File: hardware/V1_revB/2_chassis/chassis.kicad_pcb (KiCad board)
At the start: 2 copper layers, 39.1 x 31.7 mm, 18 parts, among them SW3 NKK_NR01

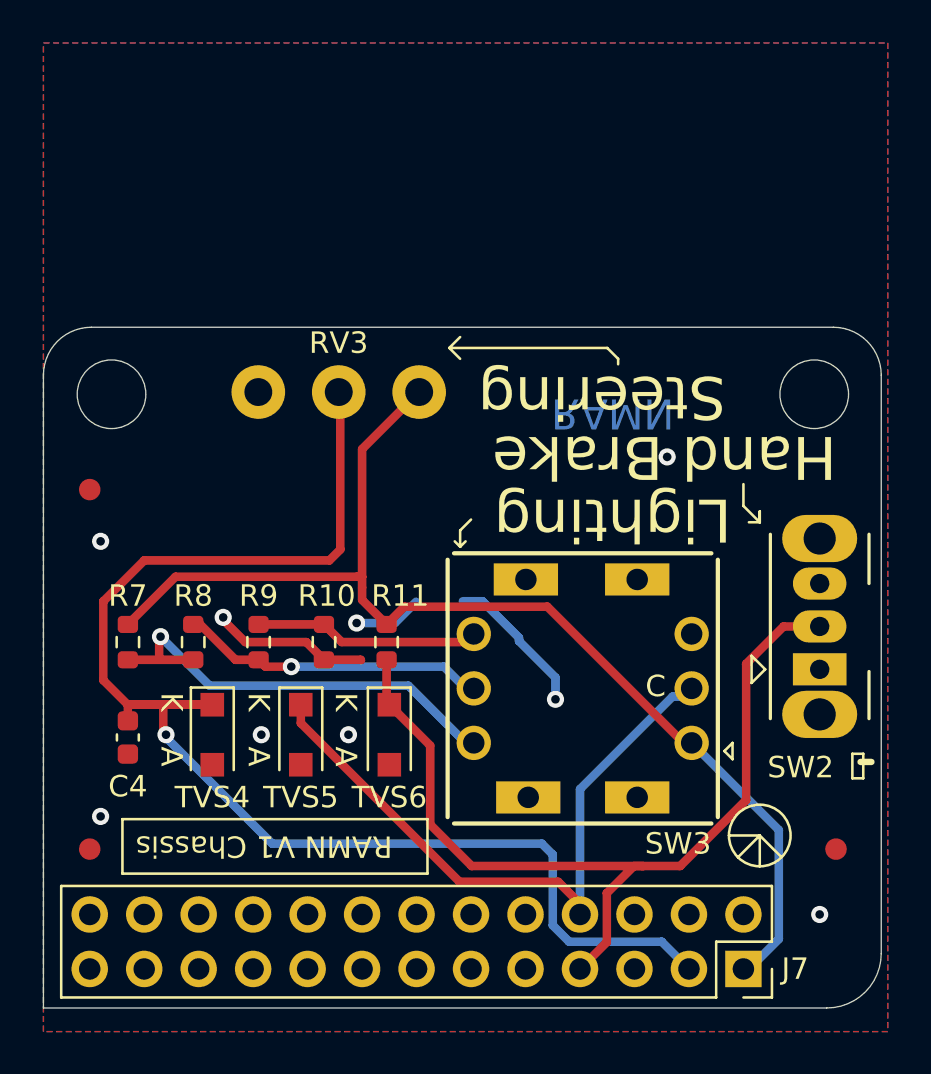
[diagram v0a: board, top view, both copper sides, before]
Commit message: Feat(Hw):Modify_footprint_Chasis_Pot
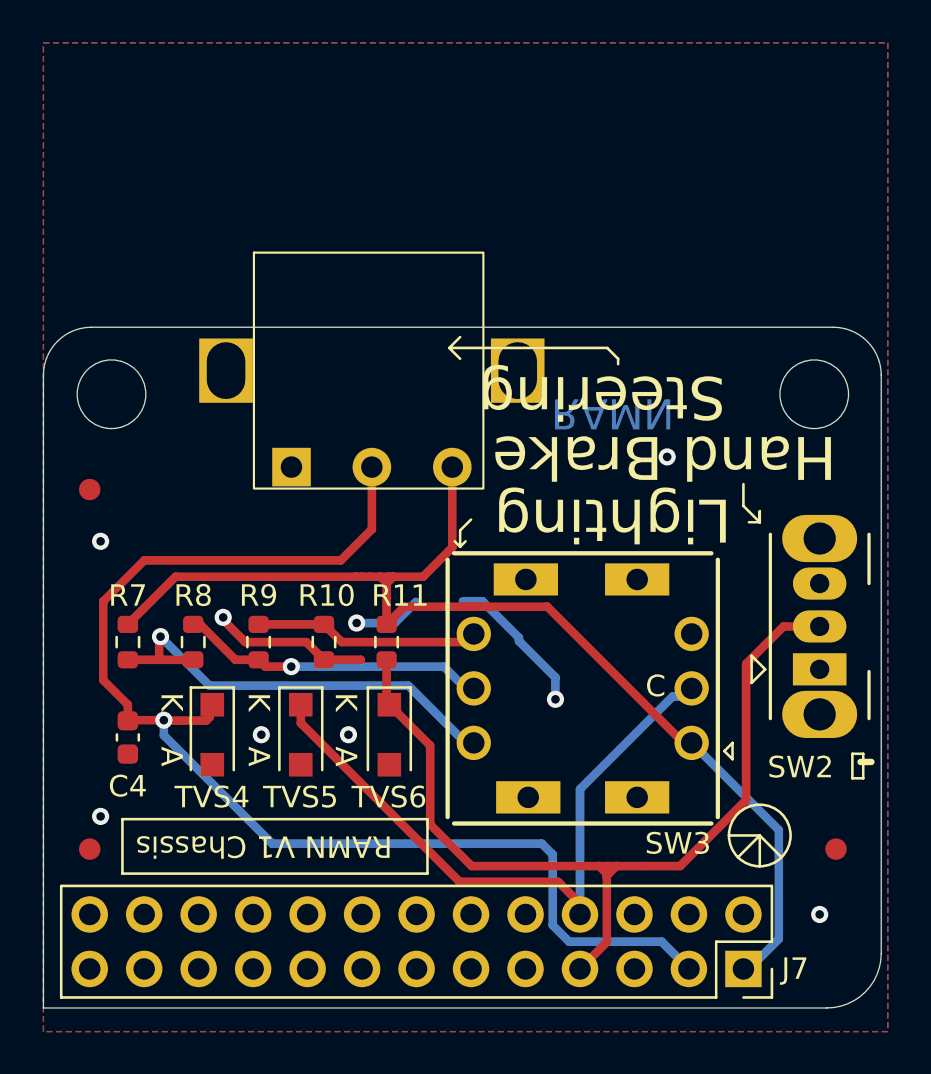
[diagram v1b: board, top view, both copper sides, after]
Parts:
- removed RV3: POT_ECU, Global_Library:POT_ECU
- added RV1: R_Potentiometer, RAMN_New_Footprint:New_Pot, F.Cu at (47.7, 35.6)
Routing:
- net Wheel: track 66.3 -> 59.2 mm

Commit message: Feat(Hw): Modify_and_fix_footprints_and_symbols
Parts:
- removed SW3: NKK_NR01, Akiyuki_UI:NR01
- added SW1: ~, RAMN_New_Footprint:NR01, F.Cu at (57.5, 50.4)
- renumbered RV1 to RV3
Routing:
- net GND: track 17.4 -> 25.9 mm

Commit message: Feat(Hw): EnhanceComponentLibraries
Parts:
- renumbered SW1 to SW3
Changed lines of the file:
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@@
 			(layers "F.Cu" "F.Mask" "F.Paste")
 			(roundrect_rratio 0.25)
-			(net "Net-(SW1-A)")
+			(net "Net-(SW3-A)")
 			(pintype "passive")
 		)
@@
 			(layers "F.Cu" "F.Mask" "F.Paste")
 			(roundrect_rratio 0.25)
-			(net "Net-(SW1-A)")
+			(net "Net-(SW3-A)")
 			(pintype "passive")
 		)
@@
 			(layers "F.Cu" "F.Mask" "F.Paste")
 			(roundrect_rratio 0.25)
-			(net "Net-(SW1-B)")
+			(net "Net-(SW3-B)")
 			(pintype "passive")
 		)
@@
 			(layers "F.Cu" "F.Mask" "F.Paste")
 			(roundrect_rratio 0.25)
-			(net "Net-(SW1-B)")
+			(net "Net-(SW3-B)")
 			(pintype "passive")
 		)
@@
 			(layers "F.Cu" "F.Mask" "F.Paste")
 			(roundrect_rratio 0.25)
-			(net "Net-(SW1-C)")
+			(net "Net-(SW3-C)")
 			(pintype "passive")
 		)
@@
 			(layers "F.Cu" "F.Mask" "F.Paste")
 			(roundrect_rratio 0.25)
-			(net "Net-(SW1-C)")
+			(net "Net-(SW3-C)")
 			(pintype "passive")
 		)
@@
 		(layer "F.Cu")
 		(at 57.531 50.419 180)
-		(property "Reference" "SW1"
+		(property "Reference" "SW3"
 			(at -4.445 -7.239 0)
 			(layer "F.SilkS")
@@
 			)
 		)
+		(property "LCSC" "C7250022"
+			(at 0 0 0)
+			(unlocked yes)
+			(layer "F.Fab")
+			(hide yes)
+			(effects
+				(font
+					(size 1 1)
+					(thickness 0.15)
+				)
+			)
+		)
 		(sheetname "/")
 		(sheetfile "chassis.kicad_sch")
@@
 			(layers "*.Cu" "*.Mask")
 			(remove_unused_layers no)
-			(net "Net-(SW1-A)")
+			(net "Net-(SW3-A)")
 			(pinfunction "A_2")
 			(pintype "input")
@@
 			(layers "*.Cu" "*.Mask")
 			(remove_unused_layers no)
-			(net "Net-(SW1-B)")
+			(net "Net-(SW3-B)")
 			(pinfunction "B_4")
 			(pintype "input")
@@
 			(layers "*.Cu" "*.Mask")
 			(remove_unused_layers no)
-			(net "Net-(SW1-C)")
+			(net "Net-(SW3-C)")
 			(pinfunction "C_6")
 			(pintype "input")
@@
 		(width 0.4)
 		(layer "F.Cu")
-		(net "Net-(SW1-A)")
+		(net "Net-(SW3-A)")
 	)
 	(segment
@@
 		(width 0.4)
 		(layer "F.Cu")
-		(net "Net-(SW1-A)")
+		(net "Net-(SW3-A)")
 	)
 	(segment
@@
 		(width 0.4)
 		(layer "F.Cu")
-		(net "Net-(SW1-A)")
+		(net "Net-(SW3-A)")
 	)
 	(segment
@@
 		(width 0.4)
 		(layer "F.Cu")
-		(net "Net-(SW1-A)")
+		(net "Net-(SW3-A)")
 	)
 	(via
@@
 		)
 		(filling no)
-		(net "Net-(SW1-A)")
+		(net "Net-(SW3-A)")
 	)
 	(segment
@@
 		(width 0.4)
 		(layer "B.Cu")
-		(net "Net-(SW1-A)")
+		(net "Net-(SW3-A)")
 	)
 	(segment
@@
 		(width 0.4)
 		(layer "B.Cu")
-		(net "Net-(SW1-A)")
+		(net "Net-(SW3-A)")
 	)
 	(segment
@@
 		(width 0.4)
 		(layer "B.Cu")
-		(net "Net-(SW1-A)")
+		(net "Net-(SW3-A)")
 	)
 	(segment
@@
 		(width 0.4)
 		(layer "F.Cu")
-		(net "Net-(SW1-B)")
+		(net "Net-(SW3-B)")
 	)
 	(segment
@@
 		(width 0.4)
 		(layer "F.Cu")
-		(net "Net-(SW1-B)")
+		(net "Net-(SW3-B)")
 	)
 	(segment
@@
 		(width 0.4)
 		(layer "F.Cu")
-		(net "Net-(SW1-B)")
+		(net "Net-(SW3-B)")
 	)
 	(segment
@@
 		(width 0.4)
 		(layer "F.Cu")
-		(net "Net-(SW1-B)")
+		(net "Net-(SW3-B)")
 	)
 	(segment
@@
 		(width 0.4)
 		(layer "F.Cu")
-		(net "Net-(SW1-B)")
+		(net "Net-(SW3-B)")
 	)
 	(via
@@
 		)
 		(filling no)
-		(net "Net-(SW1-B)")
+		(net "Net-(SW3-B)")
 	)
 	(segment
@@
 		(width 0.4)
 		(layer "B.Cu")
-		(net "Net-(SW1-B)")
+		(net "Net-(SW3-B)")
 	)
 	(segment
@@
 		(width 0.4)
 		(layer "B.Cu")
-		(net "Net-(SW1-B)")
+		(net "Net-(SW3-B)")
 	)
 	(segment
@@
 		(width 0.4)
 		(layer "F.Cu")
-		(net "Net-(SW1-C)")
+		(net "Net-(SW3-C)")
 	)
 	(segment
@@
 		(width 0.4)
 		(layer "F.Cu")
-		(net "Net-(SW1-C)")
+		(net "Net-(SW3-C)")
 	)
 	(segment
@@
 		(width 0.4)
 		(layer "F.Cu")
-		(net "Net-(SW1-C)")
+		(net "Net-(SW3-C)")
 	)
 	(zone

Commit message: Feat(Hw): UpdatePCBsToV1.2Revision
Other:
- board text added: "RAMN V1.2"
- board text removed: "RAMN"
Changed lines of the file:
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@@
 		(layer "Edge.Cuts")
 	)
-	(gr_text "RAMN"
-		(at 58.928 37.592 180)
+	(gr_text "RAMN V1.2"
+		(at 59.928 39.8 180)
 		(layer "B.Cu")
 		(effects
